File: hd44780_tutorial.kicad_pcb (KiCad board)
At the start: 2 copper layers, 157.2 x 83.5 mm, 33 parts, among them J1 LCD_2004_PinSocket_1x16_P2.54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, J2 UJC-HP-3-SMT-TR, SW1 REG SELECT, SW2 ENABLE, SW3 DS02C-254-1L-08BE

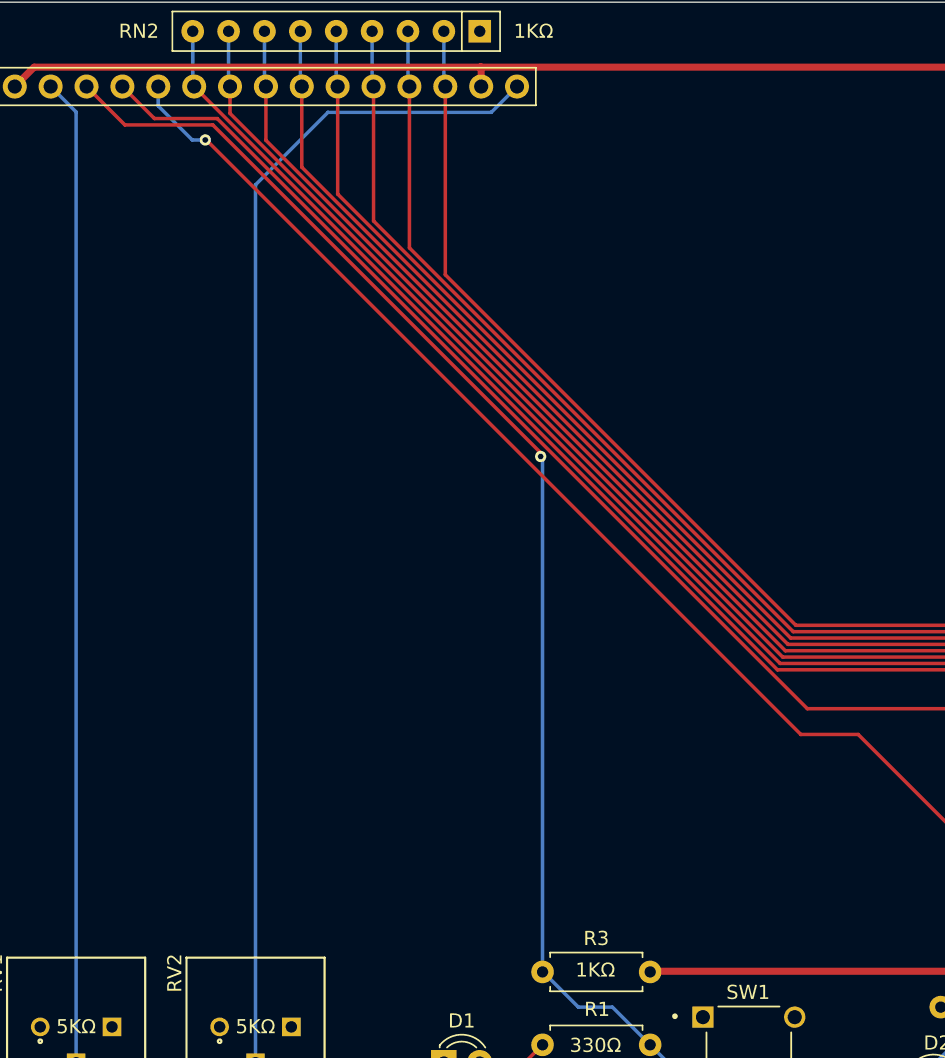
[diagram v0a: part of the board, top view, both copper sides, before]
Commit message: Changed URLs to point to Ian's web site after his suggestion. Moved the RS track so it did not need a via. Regenerated gerber/drill files. Updated front and back images.
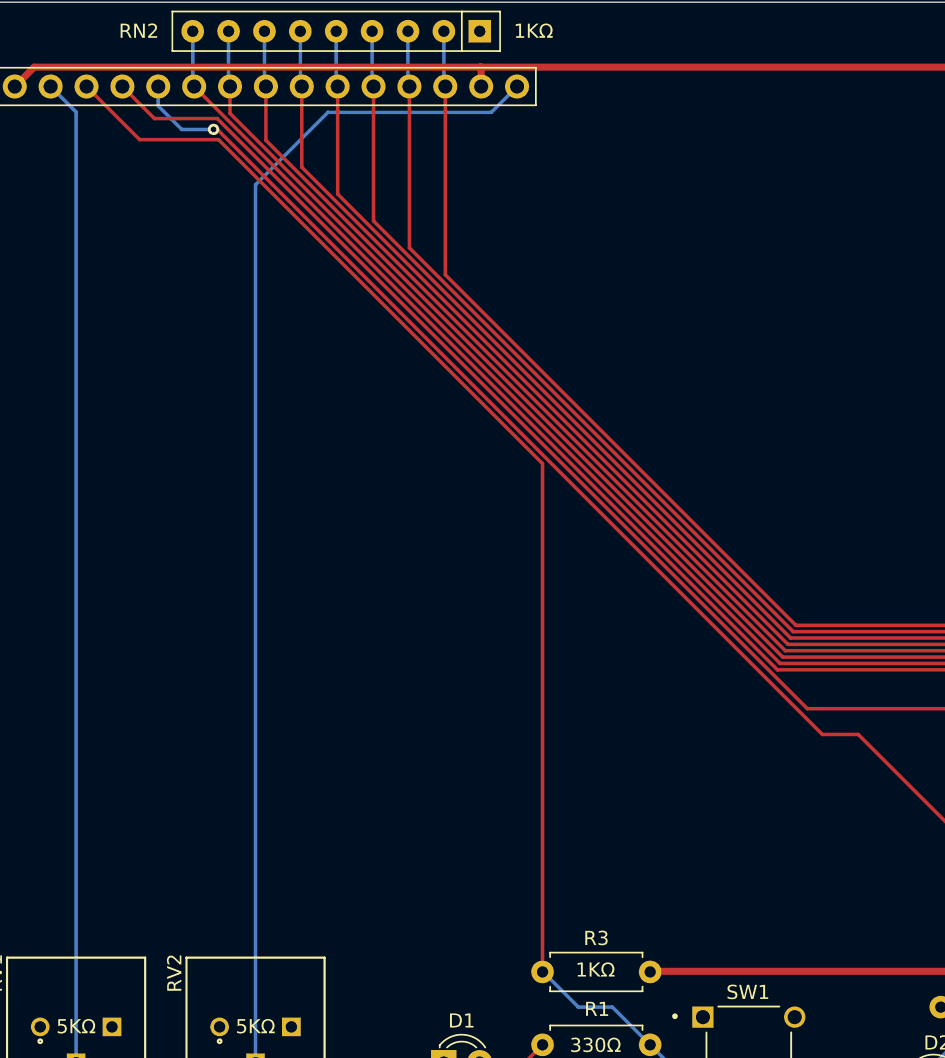
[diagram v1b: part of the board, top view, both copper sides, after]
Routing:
- net /RS: track 100.8 -> 100.4 mm, vias 1 -> 0
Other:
- board text added: "${project_name} Inspired by Ian Ward's Project: HD44780 LCD Tutorial (https://excess.org/lcd2004-tutorial/) PCB designed by an appreciative subscriber to his YouTube channel. Revision: ${version} 3/19/2024"
- board text removed: "${project_name} Inspired by Ian Ward's YouTube Video: HD44780 Tutorial (https://www.youtube.com/watch?v=Gd6GUsHL4FI) PCB designed by an appreciative subscriber to his channel. Revision: ${version} 3/17/2024"
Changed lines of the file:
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@@
   (gr_arc (start 61.2902 51.2026) (mid 62.754666 47.667066) (end 66.2902 46.2026)
     (stroke (width 0.1) (type default)) (layer "Edge.Cuts"))
-  (gr_text "${project_name}\nInspired by Ian Ward's YouTube Video: HD44780 Tutorial\n	(https://www.youtube.com/watch?v=Gd6GUsHL4FI)\nPCB designed by an appreciative subscriber to his channel.\nRevision: ${version}    3/17/2024\n" (at 196.596 67.564) (layer "B.SilkS")
+  (gr_text "${project_name}\nInspired by Ian Ward's Project: HD44780 LCD Tutorial\n	(https://excess.org/lcd2004-tutorial/)\nPCB designed by an appreciative subscriber to his YouTube channel.\nRevision: ${version}    3/19/2024\n" (at 196.596 67.564) (layer "B.SilkS")
     (effects (font (size 1.5 1.5) (thickness 0.254) bold) (justify left bottom mirror))
   )
@@
   (segment (start 208.788 72.753) (end 208.915 72.88) (width 0.5) (layer "B.Cu") (net 21))
   (segment (start 208.788 69.977) (end 208.788 72.753) (width 0.5) (layer "B.Cu") (net 21))
-  (segment (start 116.707649 78.099649) (end 93.498 54.89) (width 0.25) (layer "F.Cu") (net 22))
   (segment (start 128.195 122.555) (end 134.695 122.555) (width 0.25) (layer "F.Cu") (net 22))
-  (segment (start 93.498 54.89) (end 87.275 54.89) (width 0.25) (layer "F.Cu") (net 22))
-  (segment (start 116.707649 78.364351) (end 116.707649 78.099649) (width 0.25) (layer "F.Cu") (net 22))
-  (segment (start 87.275 54.89) (end 84.5566 52.1716) (width 0.25) (layer "F.Cu") (net 22))
-  (via (at 116.707649 78.364351) (size 0.8) (drill 0.4) (layers "F.Cu" "B.Cu") (net 22))
+  (segment (start 88.317675 55.932675) (end 84.5566 52.1716) (width 0.25) (layer "F.Cu") (net 22))
+  (segment (start 93.904279 55.932675) (end 88.317675 55.932675) (width 0.25) (layer "F.Cu") (net 22))
+  (segment (start 116.84 114.855) (end 116.84 78.868396) (width 0.25) (layer "F.Cu") (net 22))
+  (segment (start 116.84 78.868396) (end 93.904279 55.932675) (width 0.25) (layer "F.Cu") (net 22))
   (segment (start 124.46 120.015) (end 125.73 121.285) (width 0.25) (layer "B.Cu") (net 22))
   (segment (start 125.73 121.285) (end 127 121.285) (width 0.25) (layer "B.Cu") (net 22))
-  (segment (start 116.84 78.496702) (end 116.84 114.808) (width 0.25) (layer "B.Cu") (net 22))
   (segment (start 121.793 117.348) (end 124.46 120.015) (width 0.25) (layer "B.Cu") (net 22))
   (segment (start 119.38 117.348) (end 121.793 117.348) (width 0.25) (layer "B.Cu") (net 22))
@@
   (segment (start 127 121.285) (end 128.195 122.48) (width 0.25) (layer "B.Cu") (net 22))
   (segment (start 128.195 122.48) (end 128.195 122.555) (width 0.25) (layer "B.Cu") (net 22))
-  (segment (start 116.707649 78.364351) (end 116.84 78.496702) (width 0.25) (layer "B.Cu") (net 22))
   (segment (start 135.588604 96.22) (end 93.808604 54.44) (width 0.25) (layer "F.Cu") (net 23))
   (segment (start 200.025 104.775) (end 203.835 100.965) (width 0.25) (layer "F.Cu") (net 23))
@@
   (segment (start 202.1 99.525) (end 202.1 99.37) (width 0.25) (layer "F.Cu") (net 33))
   (segment (start 196.85 104.775) (end 202.1 99.525) (width 0.25) (layer "F.Cu") (net 33))
-  (segment (start 93.039 55.955) (end 135.128 98.044) (width 0.25) (layer "F.Cu") (net 34))
+  (segment (start 93.550974 55.207675) (end 93.815675 55.207675) (width 0.25) (layer "F.Cu") (net 34))
+  (segment (start 93.815675 55.207675) (end 136.652 98.044) (width 0.25) (layer "F.Cu") (net 34))
+  (segment (start 153.416 112.268) (end 153.525 112.268) (width 0.25) (layer "F.Cu") (net 34))
   (segment (start 153.525 112.268) (end 158.115 112.268) (width 0.25) (layer "F.Cu") (net 34))
-  (segment (start 135.128 98.044) (end 139.192 98.044) (width 0.25) (layer "F.Cu") (net 34))
-  (segment (start 92.964 55.955) (end 93.039 55.955) (width 0.25) (layer "F.Cu") (net 34))
-  (segment (start 153.416 112.268) (end 153.525 112.268) (width 0.25) (layer "F.Cu") (net 34))
   (segment (start 139.192 98.044) (end 153.416 112.268) (width 0.25) (layer "F.Cu") (net 34))
-  (via (at 92.964 55.955) (size 0.8) (drill 0.4) (layers "F.Cu" "B.Cu") (net 34))
-  (segment (start 92.045 55.955) (end 89.6366 53.5466) (width 0.25) (layer "B.Cu") (net 34))
+  (segment (start 136.652 98.044) (end 139.192 98.044) (width 0.25) (layer "F.Cu") (net 34))
+  (via (at 93.550974 55.207675) (size 0.8) (drill 0.4) (layers "F.Cu" "B.Cu") (net 34))
+  (segment (start 93.550974 55.207675) (end 91.297675 55.207675) (width 0.25) (layer "B.Cu") (net 34))
+  (segment (start 91.297675 55.207675) (end 89.6366 53.5466) (width 0.25) (layer "B.Cu") (net 34))
   (segment (start 89.6366 53.5466) (end 89.6366 52.1716) (width 0.25) (layer "B.Cu") (net 34))
-  (segment (start 92.964 55.955) (end 92.045 55.955) (width 0.25) (layer "B.Cu") (net 34))
   (segment (start 174.625 117.475) (end 196.065 117.475) (width 0.25) (layer "F.Cu") (net 36))
   (segment (start 206.32 107.22) (end 206.32 105.2) (width 0.25) (layer "F.Cu") (net 36))

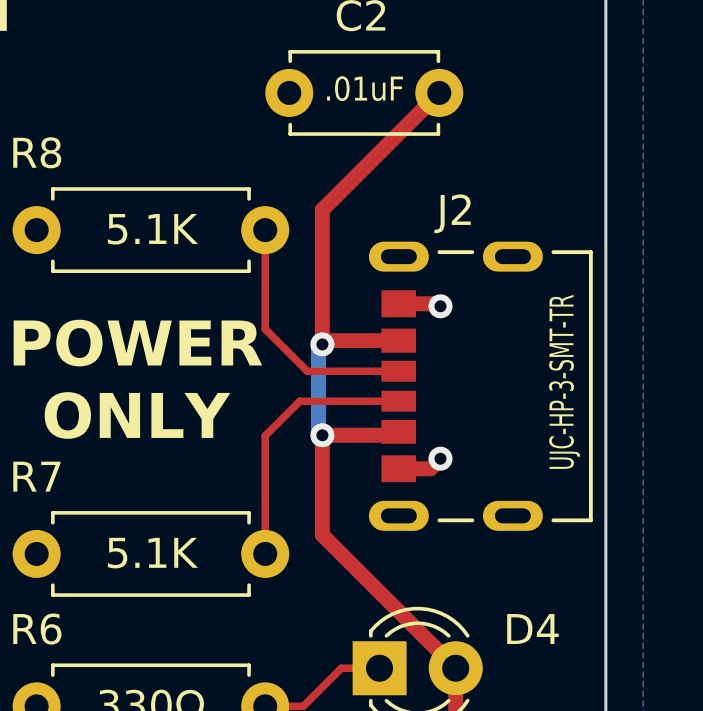
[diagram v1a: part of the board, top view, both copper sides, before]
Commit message: Moved USB connector closer to edge of board.
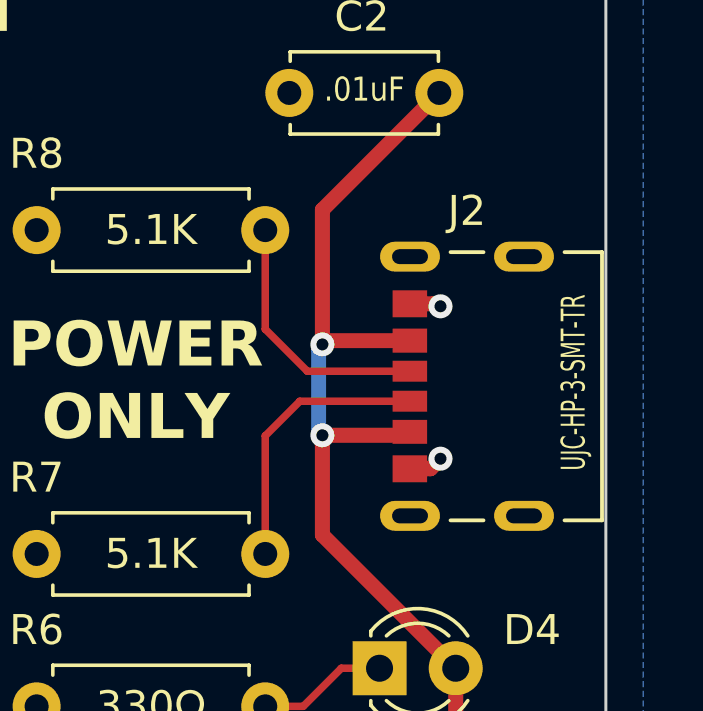
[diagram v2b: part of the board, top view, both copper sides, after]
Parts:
- moved J2 0.37 mm to (211.8, 71.2)
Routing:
- net GND: track 2.96 -> 2.22 mm
- net +5V: track 300.9 -> 301.7 mm
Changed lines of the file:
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@@
   )
   (footprint "Lutzcraft:CUI_UJC-HP-3-SMT-TR" (layer "F.Cu")
-    (at 211.465 71.245 90)
+    (at 211.836 71.245 90)
     (property "MANUFACTURER" "CUI Devices")
     (property "MAXIMUM_PACKAGE_HEIGHT" "3.16mm")
@@
     (style (thickness 0.15) (arrow_length 1.27) (text_position_mode 0) (extension_height 0.58642) (extension_offset 0.5) keep_text_aligned)
   )
-  (segment (start 212.517 73.995) (end 211.46 73.995) (width 0.5) (layer "F.Cu") (net 1))
+  (segment (start 212.517 73.995) (end 211.831 73.995) (width 0.5) (layer "F.Cu") (net 1))
   (segment (start 212.725 68.58) (end 212.64 68.495) (width 0.5) (layer "F.Cu") (net 1))
-  (segment (start 212.64 68.495) (end 211.46 68.495) (width 0.5) (layer "F.Cu") (net 1))
-  (segment (start 212.852 73.66) (end 212.517 73.995) (width 0.5) (layer "F.Cu") (net 1))
   (segment (start 212.852 68.58) (end 212.725 68.58) (width 0.5) (layer "F.Cu") (net 1))
+  (segment (start 212.64 68.495) (end 211.831 68.495) (width 0.5) (layer "F.Cu") (net 1))
+  (segment (start 212.852 73.66) (end 212.517 73.995) (width 0.5) (layer "F.Cu") (net 1))
   (via (at 212.852 73.66) (size 0.8) (drill 0.4) (layers "F.Cu" "B.Cu") (net 1))
   (via (at 212.852 68.58) (size 0.8) (drill 0.4) (layers "F.Cu" "B.Cu") (net 1))
@@
   (segment (start 209.545 80.645) (end 210.82 80.645) (width 0.25) (layer "F.Cu") (net 20))
   (segment (start 208.275 81.915) (end 209.545 80.645) (width 0.25) (layer "F.Cu") (net 20))
-  (segment (start 209.04 69.725) (end 211.46 69.725) (width 0.5) (layer "F.Cu") (net 21))
   (segment (start 213.36 80.645) (end 213.36 88.16) (width 0.5) (layer "F.Cu") (net 21))
   (segment (start 208.915 69.85) (end 208.915 65.365) (width 0.5) (layer "F.Cu") (net 21))
-  (segment (start 208.915 72.88) (end 211.345 72.88) (width 0.5) (layer "F.Cu") (net 21))
   (segment (start 213.36 88.16) (end 207.54 93.98) (width 0.5) (layer "F.Cu") (net 21))
+  (segment (start 211.716 72.88) (end 211.831 72.765) (width 0.5) (layer "F.Cu") (net 21))
   (segment (start 164.084 50.8) (end 80.8482 50.8) (width 0.5) (layer "F.Cu") (net 21))
   (segment (start 208.915 76.2) (end 213.36 80.645) (width 0.5) (layer "F.Cu") (net 21))
@@
   (segment (start 208.915 65.365) (end 212.812 61.468) (width 0.5) (layer "F.Cu") (net 21))
   (segment (start 210.32 102.735) (end 208.32 104.735) (width 0.5) (layer "F.Cu") (net 21))
+  (segment (start 209.04 69.725) (end 211.831 69.725) (width 0.5) (layer "F.Cu") (net 21))
+  (segment (start 208.915 72.88) (end 211.716 72.88) (width 0.5) (layer "F.Cu") (net 21))
   (segment (start 155.878 114.808) (end 159.31 118.24) (width 0.5) (layer "F.Cu") (net 21))
   (segment (start 210.32 100.2) (end 210.32 102.735) (width 0.5) (layer "F.Cu") (net 21))
@@
   (segment (start 167.64 119.888) (end 200.787 119.888) (width 0.5) (layer "F.Cu") (net 21))
   (segment (start 165.81 118.24) (end 165.992 118.24) (width 0.5) (layer "F.Cu") (net 21))
-  (segment (start 211.345 72.88) (end 211.46 72.765) (width 0.5) (layer "F.Cu") (net 21))
   (segment (start 208.915 69.85) (end 209.04 69.725) (width 0.5) (layer "F.Cu") (net 21))
   (segment (start 165.992 118.24) (end 167.64 119.888) (width 0.5) (layer "F.Cu") (net 21))
@@
   (segment (start 115.0366 52.1716) (end 113.2082 54) (width 0.25) (layer "B.Cu") (net 24))
   (segment (start 101.65 54) (end 96.52 59.13) (width 0.25) (layer "B.Cu") (net 24))
-  (segment (start 208.163 71.745) (end 211.46 71.745) (width 0.25) (layer "F.Cu") (net 25))
   (segment (start 207.01 72.898) (end 208.163 71.745) (width 0.25) (layer "F.Cu") (net 25))
   (segment (start 207.01 76.835) (end 207.01 72.898) (width 0.25) (layer "F.Cu") (net 25))
-  (segment (start 207.01 69.342) (end 208.413 70.745) (width 0.25) (layer "F.Cu") (net 26))
+  (segment (start 208.163 71.745) (end 211.831 71.745) (width 0.25) (layer "F.Cu") (net 25))
   (segment (start 207.01 66.04) (end 207.01 69.342) (width 0.25) (layer "F.Cu") (net 26))
-  (segment (start 208.413 70.745) (end 211.46 70.745) (width 0.25) (layer "F.Cu") (net 26))
+  (segment (start 207.01 69.342) (end 208.413 70.745) (width 0.25) (layer "F.Cu") (net 26))
+  (segment (start 208.413 70.745) (end 211.831 70.745) (width 0.25) (layer "F.Cu") (net 26))
   (segment (start 82.0166 52.1716) (end 83.82 53.975) (width 0.25) (layer "B.Cu") (net 31))
   (segment (start 83.82 53.975) (end 83.82 121.285) (width 0.25) (layer "B.Cu") (net 31))
